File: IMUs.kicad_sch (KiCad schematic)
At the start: 15 parts, among them U501 LSM6DSL, U502 DPS368

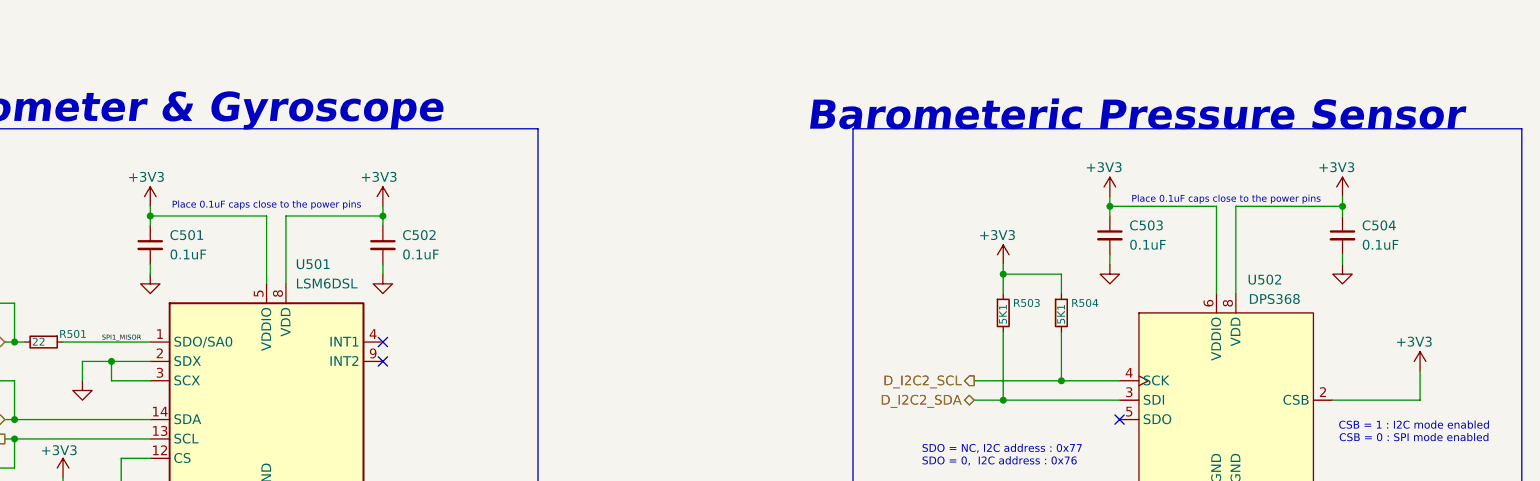
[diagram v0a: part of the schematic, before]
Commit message: refactor: change tim5 ch 1 label to ch 2
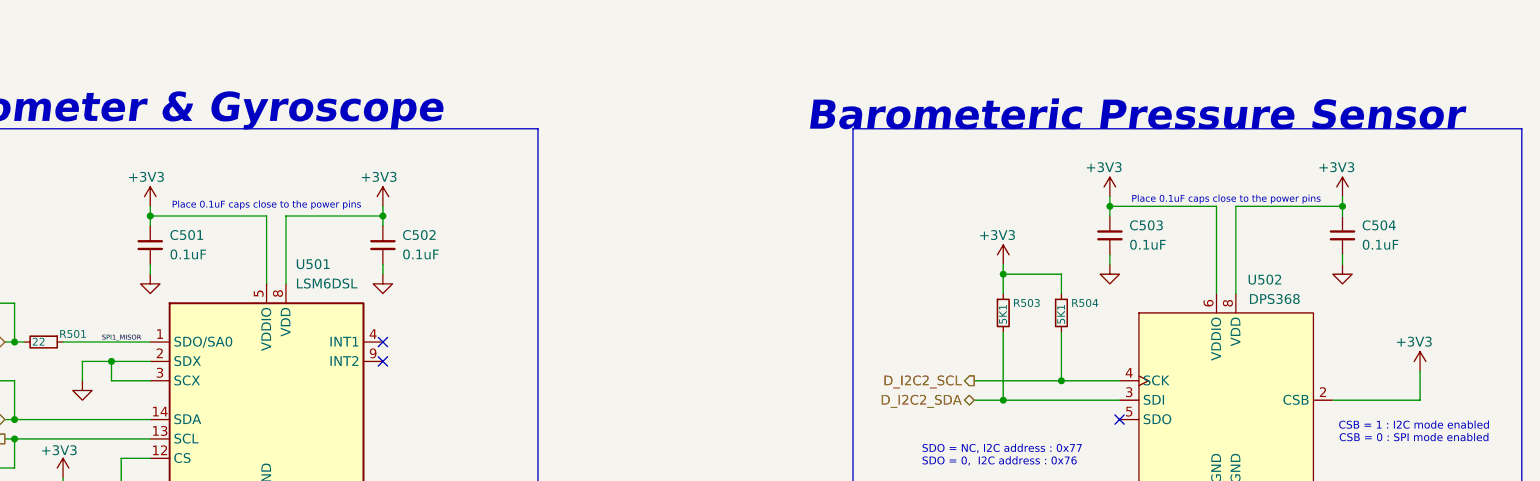
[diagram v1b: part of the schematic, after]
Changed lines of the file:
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@@
 		(fields_autoplaced yes)
 		(property "Reference" "C502"
-			(at 111.76 72.3962 0)
+			(at 111.76 72.3899 0)
 			(show_name no)
 			(do_not_autoplace no)
@@
 		)
 		(property "Value" "0.1uF"
-			(at 111.76 74.9362 0)
+			(at 111.76 74.9299 0)
 			(show_name no)
 			(do_not_autoplace no)
@@
 		)
 		(property "Description" "Unpolarized capacitor, small symbol"
-			(at 109.22 73.66 0)
+			(at 109.22 83.82 0)
 			(hide yes)
 			(show_name no)
@@
 		(fields_autoplaced yes)
 		(property "Reference" "C503"
-			(at 207.01 71.1262 0)
+			(at 207.01 71.1199 0)
 			(show_name no)
 			(do_not_autoplace no)
@@
 		)
 		(property "Value" "0.1uF"
-			(at 207.01 73.6662 0)
+			(at 207.01 73.6599 0)
 			(show_name no)
 			(do_not_autoplace no)
@@
 		)
 		(property "Description" "Unpolarized capacitor, small symbol"
-			(at 204.47 72.39 0)
+			(at 204.47 82.55 0)
 			(hide yes)
 			(show_name no)
@@
 		(fields_autoplaced yes)
 		(property "Reference" "C501"
-			(at 81.28 72.3962 0)
+			(at 81.28 72.3899 0)
 			(show_name no)
 			(do_not_autoplace no)
@@
 		)
 		(property "Value" "0.1uF"
-			(at 81.28 74.9362 0)
+			(at 81.28 74.9299 0)
 			(show_name no)
 			(do_not_autoplace no)
@@
 		)
 		(property "Description" "Unpolarized capacitor, small symbol"
-			(at 78.74 73.66 0)
+			(at 78.74 83.82 0)
 			(hide yes)
 			(show_name no)
@@
 		(fields_autoplaced yes)
 		(property "Reference" "C504"
-			(at 237.49 71.1262 0)
+			(at 237.49 71.1199 0)
 			(show_name no)
 			(do_not_autoplace no)
@@
 		)
 		(property "Value" "0.1uF"
-			(at 237.49 73.6662 0)
+			(at 237.49 73.6599 0)
 			(show_name no)
 			(do_not_autoplace no)
@@
 		)
 		(property "Description" "Unpolarized capacitor, small symbol"
-			(at 234.95 72.39 0)
-			(hide yes)
-			(show_name no)
+			(at 234.95 82.55 0)
+			(hide yes)
+			(show_name no)
